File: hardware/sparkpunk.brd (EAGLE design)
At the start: 88.9 x 63.5 mm, 71 parts, among them IC1 556, IC2 CD4013B, IC3 LM358, IC4 LM358, J1 AUDIO-JACK2KIT

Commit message: Updates following group review
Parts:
- moved FRAME1 9.92 mm to (24.1, -12.7)
- moved C7 1.27 mm to (57.1, 34.3)
- moved RV2 1.27 mm to (8.89, 50.8)
- moved RV3 1.27 mm to (8.89, 12.7)
- moved C3 1.27 mm to (61.0, 45.7)
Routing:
- net N$31: track 59.7 -> 66.8 mm, vias 0 -> 1
- net PITCH2: track 99.8 -> 106.5 mm
- net PITCH1: track 88.7 -> 95.3 mm
- net VCC: track 226.8 -> 223.3 mm
- net N$12: track 12.9 -> 14.9 mm
- net PTICH1: track 27.2 -> 28.8 mm
- net N$13: track 14.1 -> 12.8 mm
- net N$22: track 9.42 -> 8.15 mm
- net N$21: track 25.7 -> 27.0 mm
- net N$33: track 77.5 -> 78.3 mm, vias 1 -> 0
- net N$8: track 8.26 -> 8.84 mm
- net N$18: track 23.9 -> 24.4 mm
- net SUB1: track 59.4 -> 58.8 mm
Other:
- board text added: "IN"
- board text added: "V+"
- board text added: "V-"
- board text added: "Vcc"
- board text added: "Vin"

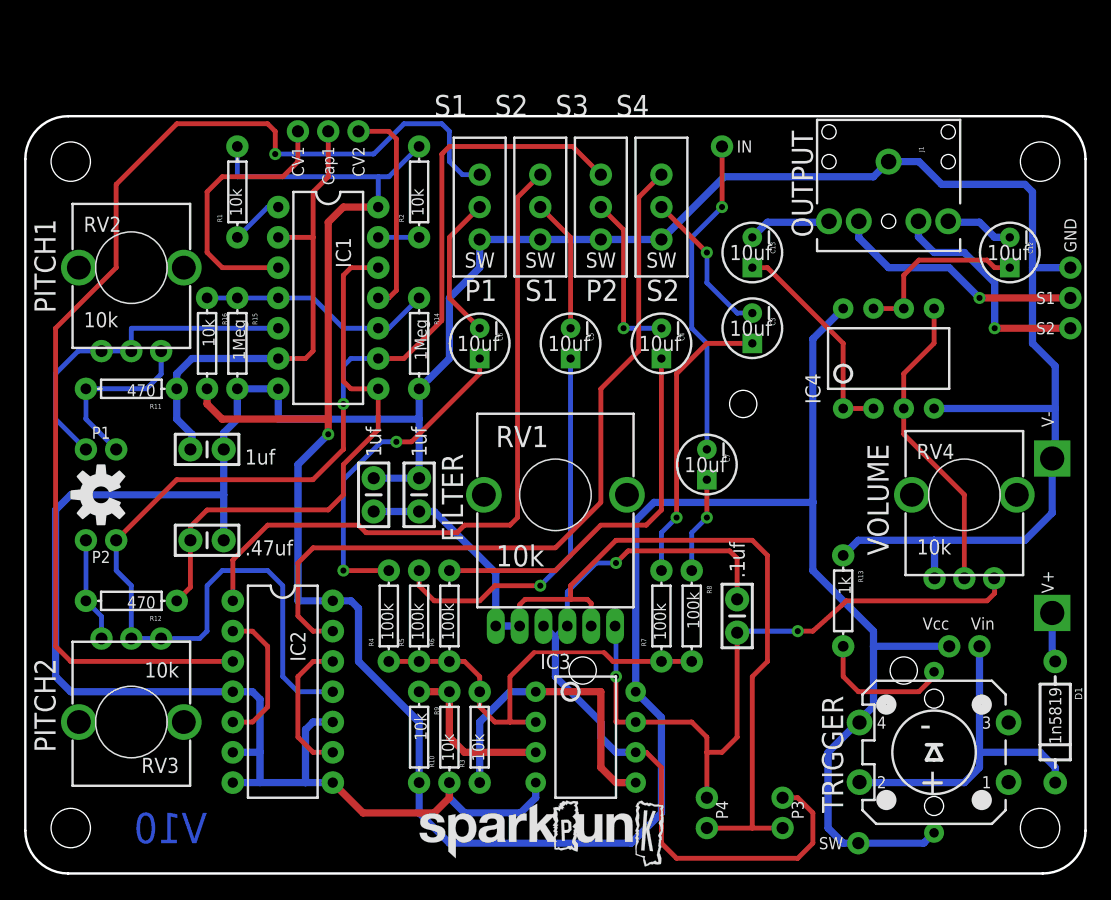
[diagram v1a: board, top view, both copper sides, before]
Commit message: Updates from prototype evaluation
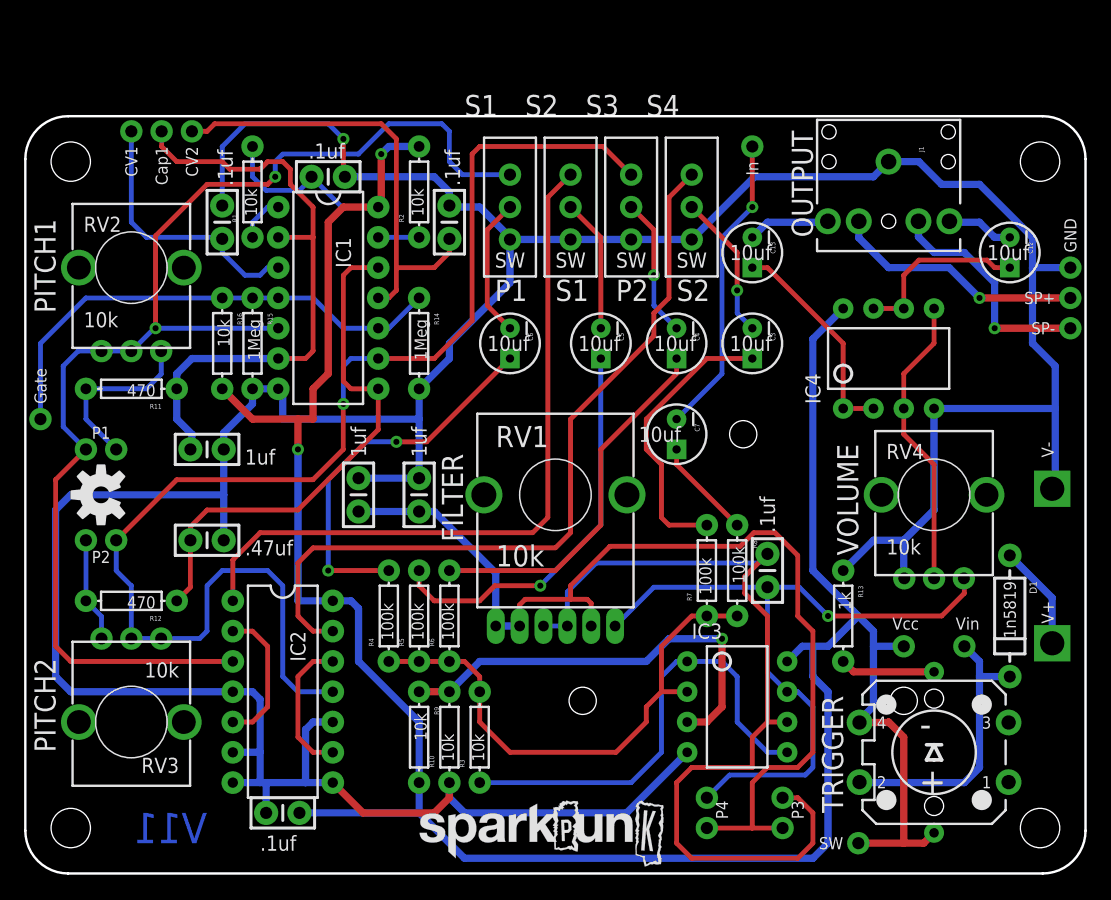
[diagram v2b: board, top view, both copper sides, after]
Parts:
- added C10, C14, C15, C16: .1uf, SparkFun-Capacitors:CAP-PTH-SMALL-KIT
- added GATE: CV2, SparkFun-Connectors:1X01NS
- IC1: value 556 -> 7556
- moved JP2 14.0 mm to (14.0, 62.2)
- moved JP1 14.0 mm to (8.89, 62.2)
- moved JP4 14.0 mm to (11.4, 62.2)
- moved IC3 13.0 mm to (59.7, 14.0)
- moved D1 9.67 mm to (82.5, 21.6)
- moved R7 5.39 mm to (57.1, 25.4)
- moved R8 5.39 mm to (59.7, 25.4)
- moved C11 4.58 mm to (62.2, 25.4)
- moved JP16 3.81 mm to (73.7, 19.1)
- moved C7 3.59 mm to (54.6, 36.8)
- moved BAT1 2.54 mm to (33.0, 40.6)
- moved C5 2.54 mm to (48.3, 44.5)
- moved C6 2.54 mm to (40.6, 44.5)
- moved JP3 2.54 mm to (61.0, 61.0)
- moved S1 2.54 mm to (40.6, 55.9)
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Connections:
- removed net N$7: IC1.3, JP1.1
- removed net N$9: IC1.11, JP2.1
- removed net PTICH1: IC1.5, JP11.1, RV2.P$1, RV2.P$2
- new net VCC1: C10.1, IC1.11, JP2.1
- new net VCC2: C14.1, IC1.3, JP1.1
- net GND: now also C10.2, C14.2, C15.2, C16.2
- net N$4: now also GATE.1
- net PITCH1: now also IC1.5, JP11.1, RV2.P$1, RV2.P$2
- net VCC: now also C15.1, C16.1
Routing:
- net GND: track 265.0 -> 311.1 mm, vias 0 -> 1
- net VCC1: track 0.00 -> 38.5 mm
- net PTICH1: track 28.8 -> 0.00 mm
- net N$7: track 22.8 -> 0.00 mm
- net VCC2: track 0.00 -> 22.7 mm
- net VREF: track 14.1 -> 36.4 mm, vias 0 -> 1
- net N$4: track 19.9 -> 41.8 mm
- net N$9: track 17.9 -> 0.00 mm
- net N$27: track 26.1 -> 39.1 mm
- net VCAP1: track 41.0 -> 51.5 mm
- net PITCH1: track 95.3 -> 105.4 mm, vias 1 -> 2
- net N$26: track 36.1 -> 44.5 mm
- net N$33: track 78.3 -> 86.3 mm
- net N$31: track 66.8 -> 74.7 mm, vias 1 -> 0
- net N$1: track 28.9 -> 23.8 mm
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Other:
- board text added: "Gate"
- board text added: "In"
- board text added: "SP+"
- board text added: "SP-"
- board text added: "V11"
- board text removed: "IN"
- board text removed: "V10"

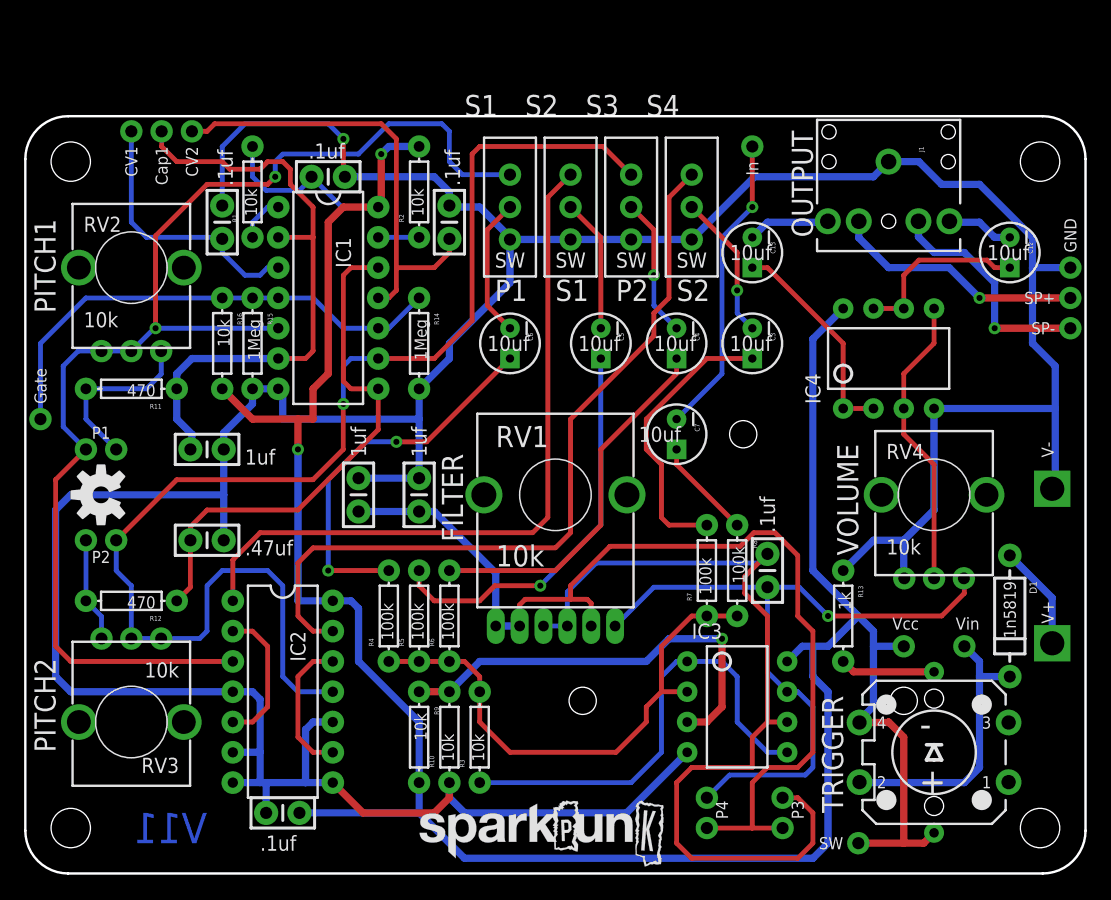
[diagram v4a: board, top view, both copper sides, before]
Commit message: PCB update
Redesigned some aspects of PCB, for tighter integration with the
sequencer.
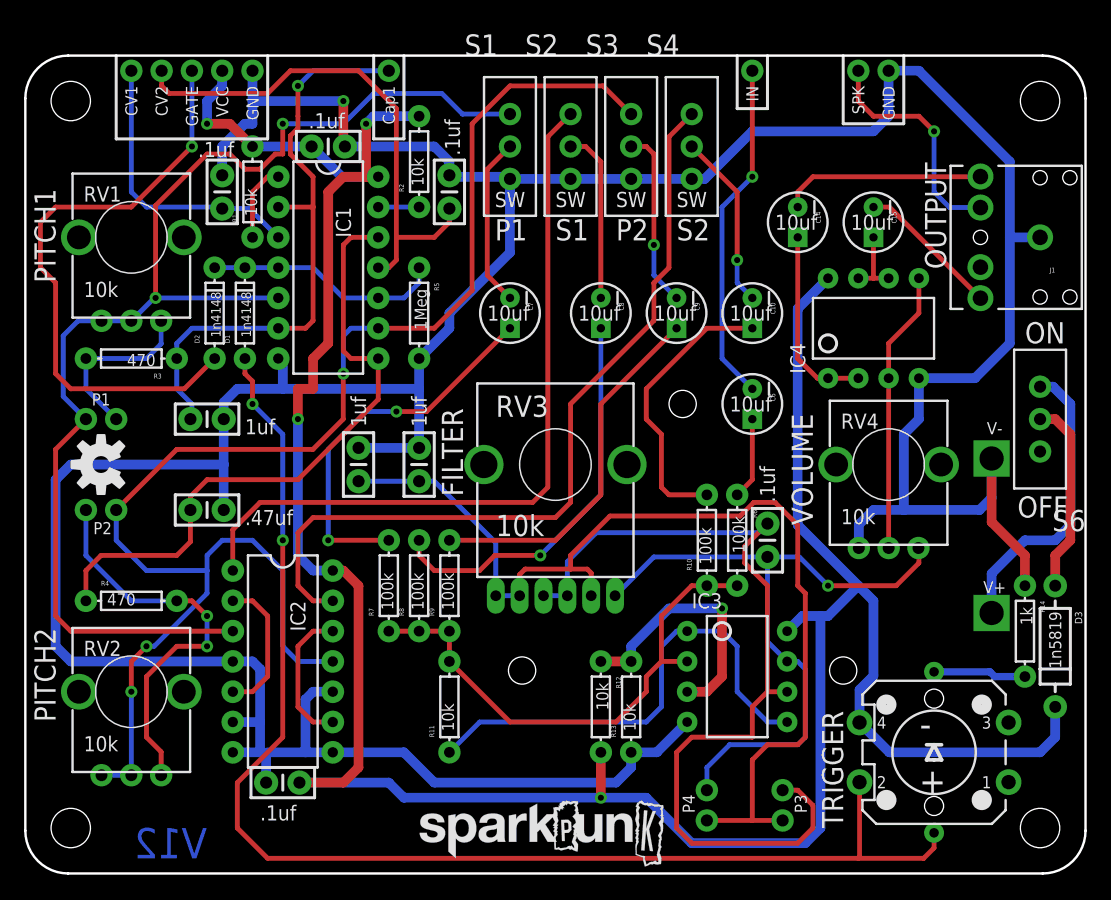
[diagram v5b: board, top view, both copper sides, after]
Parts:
- removed GATE: CV2, SparkFun-Connectors:1X01NS
- removed JP18: Vin, SparkFun-Connectors:1X01NS
- removed R15: 1Meg, SparkFun-Resistors:AXIAL-0.3EZ
- removed R16: 10k, SparkFun-Resistors:AXIAL-0.3EZ
- added D2: 1n4148, SparkFun-DiscreteSemi:DIODE-1N4148-KIT
- added D3: 1n5819, SparkFun-DiscreteSemi:DIODE-1N4001
- added S6: SPDT, SparkFun-Electromechanical:SWITCH-SPDT_KIT
- C1: value .47uf -> .1uf
- C10, C14, C15: value .1uf -> 10uf/25V; device SparkFun-Capacitors:CAP-PTH-SMALL-KIT -> SparkFun-Capacitors:CPOL-RADIAL-10UF-25V-KIT
- C12, C13, C3: value 10uf/25V -> 1uf; device SparkFun-Capacitors:CPOL-RADIAL-10UF-25V-KIT -> SparkFun-Capacitors:CAP-PTH-SMALL-KIT
- C2: value 1uf -> .1uf
- C4: value 10uf/25V -> .47uf; device SparkFun-Capacitors:CPOL-RADIAL-10UF-25V-KIT -> SparkFun-Capacitors:CAP-PTH-SMALL-KIT
- C5: value 10uf/25V -> .1uf; device SparkFun-Capacitors:CPOL-RADIAL-10UF-25V-KIT -> SparkFun-Capacitors:CAP-PTH-SMALL-KIT
- C8, C9: value 1uf -> 10uf/25V; device SparkFun-Capacitors:CAP-PTH-SMALL-KIT -> SparkFun-Capacitors:CPOL-RADIAL-10UF-25V-KIT
- D1: value 1n5819 -> 1n4148; device SparkFun-DiscreteSemi:DIODE-1N4001 -> SparkFun-DiscreteSemi:DIODE-1N4148-KIT
- JP11: value P1 -> P3
- JP12: value P1 -> P4
- JP13: value P2 -> P4
- JP14: value P2 -> SPK
- JP17: value Vsw -> GND
- JP3: value IN -> P1
- JP4: value CAP1 -> P1
- JP5: value S1 -> P2
- JP6: value S2 -> P2
- JP7: value P4 -> CAP1
- JP8: value P4 -> GATE
- JP9: value P3 -> IN
- R10, R9: value 10k -> 100k
- R11, R12: value 470 -> 10k
- R13: value 1k -> 10k
- R14: value 1Meg -> 1k
- R3: value 10k -> 470
- R4: value 100k -> 470
- R5: value 100k -> 1Meg
- RV1: device SparkFun-Electromechanical:POT_PANASONIC_DUAL_VERT_KIT -> SparkFun-Electromechanical:ALPS_POT_KIT
- RV3: device SparkFun-Electromechanical:ALPS_POT_KIT -> SparkFun-Electromechanical:POT_PANASONIC_DUAL_VERT_KIT
- moved JP6 83.9 mm to (5.08, 30.5), turned to 0 degrees
- moved JP17 82.3 mm to (19.1, 67.3)
- moved JP5 82.0 mm to (7.62, 30.5), turned to 0 degrees
- moved JP8 76.8 mm to (14.0, 67.3), turned to 0 degrees
- moved JP14 75.8 mm to (69.8, 67.3), turned to 90 degrees
- moved JP16 74.8 mm to (16.5, 67.3)
- moved D1 69.0 mm to (18.4, 47.0), turned to 90 degrees
- moved JP7 66.5 mm to (30.5, 67.3), turned to 0 degrees
- moved JP11 66.2 mm to (63.5, 4.45), turned to 180 degrees
- moved JP9 61.0 mm to (61.0, 67.3), turned to 0 degrees
- moved JP3 60.4 mm to (5.08, 38.1)
- moved JP12 58.5 mm to (57.1, 4.45), turned to 180 degrees
- moved C12 57.4 mm to (27.9, 34.3)
- moved R14 56.2 mm to (83.8, 20.3)
- moved JP13 53.8 mm to (57.1, 6.99), turned to 180 degrees
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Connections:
- removed net N$15: J1.RSH, JP6.1
- removed net N$6: R13.P$2, S5.C
- new net BUTTON: D1.A, S5.2, S5.A
- new net N$7: D3.A, S6.2
- new net N$9: R14.P$2, S5.C
- net FILT-OUT: now also JP13.1, RV3.A3; no longer JP7.1, RV1.A3
- net GND: now also C12.1, C13.2, C2.2, C3.1, C4.2, C5.2, JP17.1, R14.P$1, R5.P$2; no longer C10.2, C14.2, C15.2, C2.1, C8.1, C9.2, R10.P$1, R14.P$2, R15.P$2
- net N$1: now also D2.A, JP8.1; no longer D1.C, JP18.1, S5.2
- net N$12: now also JP4.1, R3.P$2, RV1.P$3; no longer JP12.1, R11.P$2, RV2.P$3
- net N$13: now also C10.2; no longer C3.2
- net N$14: now also JP14.1; no longer JP5.1
- net N$16: now also C14.1; no longer C13.1
- net N$17: now also C15.2; no longer C12.2
- net N$18: now also C10.1, R10.P$2; no longer C3.1, R7.P$2
- net N$19: now also C9.1, R9.P$2; no longer C4.1, R6.P$2
- net N$20: now also C9.2; no longer C4.2
- net N$21: now also C6.2, JP9.1; no longer C7.2, JP3.1
- net N$22: now also C6.1, R6.P$1; no longer C7.1, R8.P$1
- net N$23: now also C7.2; no longer C6.2
- net N$24: now also C8.2; no longer C5.2
- net N$25: now also C15.1; no longer C12.1
- net N$26: now also R10.P$1, R11.P$2, R6.P$2, R8.P$1, R9.P$1; no longer R3.P$2, R4.P$1, R5.P$1, R6.P$1, R8.P$2
- net N$27: now also R11.P$1; no longer R3.P$1
- net N$28: now also C8.1, R8.P$2; no longer C5.1, R5.P$2
- net N$29: now also C7.1, R7.P$2; no longer C6.1, R4.P$2
- net N$3: now also C4.1, R4.P$1; no longer C1.1, R12.P$1
- net N$30: now also C14.2; no longer C13.2
- net N$31: now also JP10.1, RV3.B1, RV3.B2; no longer JP9.1, RV1.B1, RV1.B2
- net N$33: now also C12.2, C13.1, JP11.1, JP12.1, RV3.A1, RV3.A2, RV3.B3; no longer C8.2, C9.1, JP10.1, JP8.1, RV1.A1, RV1.A2, RV1.B3
- net N$4: now also D1.C, D2.C, R5.P$1; no longer GATE.1, R14.P$1, R15.P$1, R16.P$1
- net N$8: now also JP6.1, R4.P$2, RV2.P$3; no longer JP14.1, R12.P$2, RV3.P$3
- net PITCH1: now also JP3.1, RV1.P$1, RV1.P$2; no longer JP11.1, RV2.P$1, RV2.P$2
- net PITCH2: now also JP5.1, RV2.P$1, RV2.P$2; no longer JP13.1, RV3.P$1, RV3.P$2
- net VBATT: now also S6.3; no longer D1.A
- net VCAP1: now also C3.2, JP7.1, R3.P$1; no longer C2.2, JP4.1, R11.P$1
- net VCC: now also C5.1, D3.C, R12.P$2; no longer C15.1, JP17.1, R16.P$2, R9.P$2, S5.A
- net VCC1: now also C2.1; no longer C10.1
- net VCC2: now also C1.1; no longer C14.1
- net VREF: now also R12.P$1, R13.P$2; no longer R10.P$2, R9.P$1
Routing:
- net BUTTON: track 0.00 -> 109.8 mm, vias 0 -> 2
- net N$1: track 23.8 -> 49.8 mm, vias 0 -> 1
- net N$8: track 8.84 -> 33.5 mm, vias 0 -> 2
- net N$4: track 41.8 -> 20.0 mm
- net N$15: track 19.5 -> 0.00 mm, vias 1 -> 0
- net PITCH2: track 109.0 -> 125.4 mm, vias 1 -> 3
- net N$7: track 0.00 -> 16.3 mm
- net VBATT: track 8.84 -> 24.9 mm
- net VREF: track 36.4 -> 21.9 mm
- net GND: track 311.1 -> 324.8 mm
- net N$30: track 6.89 -> 17.1 mm
- net N$3: track 44.5 -> 53.9 mm
- net N$25: track 15.0 -> 5.97 mm
- net N$6: track 7.98 -> 0.00 mm
- net N$9: track 0.00 -> 7.79 mm
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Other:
- board size 88.9 x 63.5 mm -> 88.9 x 68.6 mm
- board text added: "GATE"
- board text added: "IN"
- board text added: "OFF"
- board text added: "ON"
- board text added: "SPK"
- board text added: "V12"
- board text added: "VCC"
- board text removed: "Gate"
- board text removed: "In"
- board text removed: "SP+"
- board text removed: "SP-"
- board text removed: "V11"
- board text removed: "Vcc"
- board text removed: "Vin"

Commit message: Updated with feedback from beta builders.
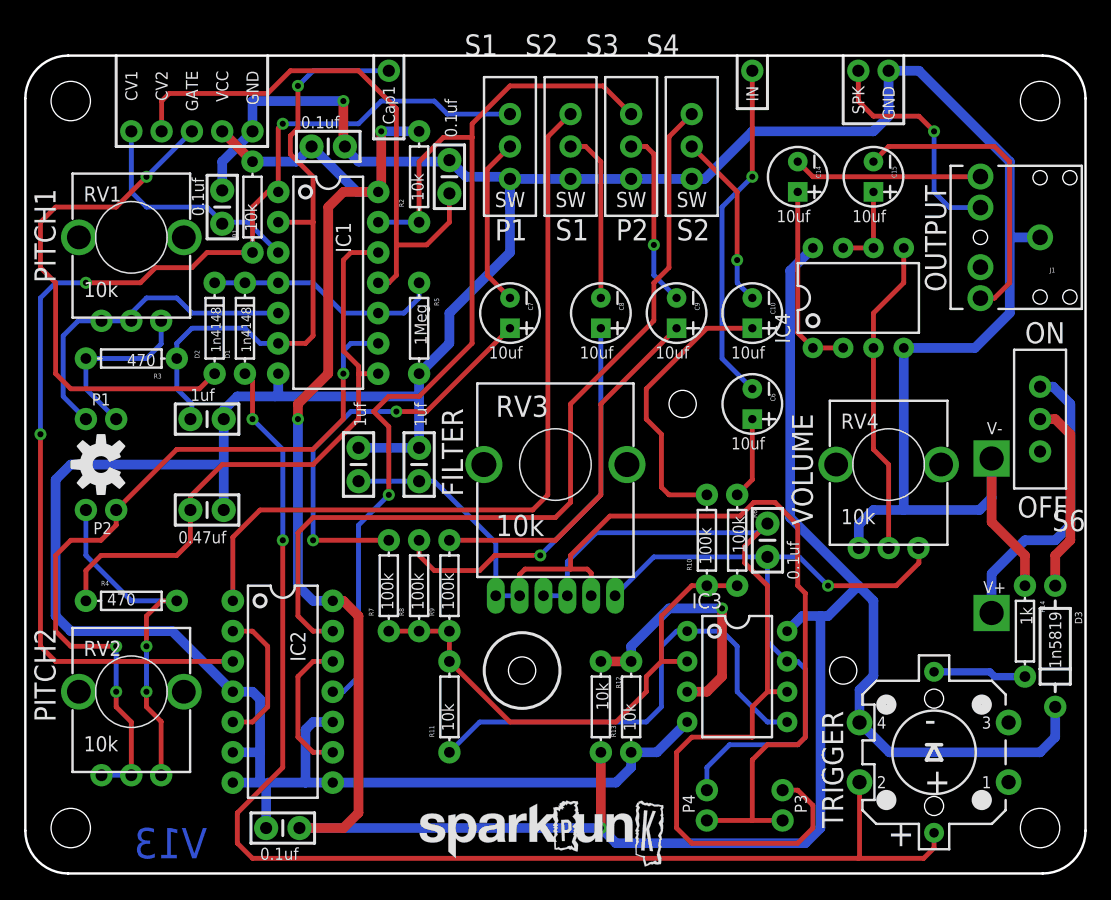
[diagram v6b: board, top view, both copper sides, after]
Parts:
- BAT1: device SparkFun-Connectors:BC9VPC -> SparkFun-Connectors:BC9VPC_KIT
- D3: device SparkFun-DiscreteSemi:DIODE-1N4001 -> SparkFun-DiscreteSemi:DIODE-1N4001-KIT
- moved JP1 5.08 mm to (8.89, 62.2)
- moved JP16 5.08 mm to (16.5, 62.2)
- moved JP17 5.08 mm to (19.1, 62.2)
- moved JP2 5.08 mm to (11.4, 62.2)
- moved JP8 5.08 mm to (14.0, 62.2)
- moved C14 3.81 mm to (64.8, 58.4)
- moved C15 3.81 mm to (71.1, 58.4)
- moved C16 3.81 mm to (21.6, 3.81)
- moved IC4 2.84 mm to (69.8, 48.3)
- moved IC2 2.54 mm to (21.6, 14.0)
- moved C2 1.27 mm to (35.6, 58.4)
- moved D1 1.27 mm to (18.4, 45.7)
- moved D2 1.27 mm to (15.9, 45.7)
- moved IC1 1.27 mm to (25.4, 48.3)
- moved R5 1.27 mm to (33.0, 45.7)
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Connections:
- removed net N$2: IC1.1, R1.P$1
- removed net N$5: IC1.13, R2.P$1
- new net POT1: IC1.5, JP3.1, RV1.P$1, RV1.P$2
- new net POT2: IC1.9, JP5.1, RV2.P$1, RV2.P$2
- net PITCH1: now also IC1.1, R1.P$1; no longer IC1.5, JP3.1, RV1.P$1, RV1.P$2
- net PITCH2: now also IC1.13, R2.P$1; no longer IC1.9, JP5.1, RV2.P$1, RV2.P$2
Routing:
- net POT2: track 0.00 -> 64.3 mm, vias 0 -> 3
- net PITCH2: track 125.4 -> 84.9 mm, vias 3 -> 1
- net POT1: track 0.00 -> 28.0 mm
- net N$17: track 12.1 -> 25.6 mm
- net PITCH1: track 104.7 -> 97.9 mm, vias 2 -> 3
- net N$2: track 6.50 -> 0.00 mm
- net N$1: track 49.8 -> 43.5 mm
- net VCC2: track 24.1 -> 19.7 mm
- net VCC1: track 43.9 -> 48.0 mm
- net N$8: track 33.5 -> 29.9 mm
- net N$5: track 3.43 -> 0.00 mm
- net N: track 23.7 -> 26.7 mm
- net GND: track 324.8 -> 321.9 mm
- net SUB1: track 63.4 -> 65.9 mm
- net N$29: track 32.1 -> 34.7 mm
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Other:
- board text added: "0.1uf"
- board text added: "0.47uf"
- board text added: "V13"
- board text removed: ".1uf"
- board text removed: ".47uf"
- board text removed: "V12"
